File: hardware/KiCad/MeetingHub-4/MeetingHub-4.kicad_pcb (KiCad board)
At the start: 4 copper layers, 265 x 160 mm, 75 parts, among them J1 USB-C POWER IN, J2 TRRS Notebook 1, J3 TRRS Notebook 2, J4 TRRS Notebook 3, J5 TRRS Notebook 4, J6 Headset (User), K1 Select NB1, K2 Select NB2, K3 Select NB3, K4 Select NB4, SW1 MUTE, SW2 Select NB1, SW3 Select NB2, SW4 Select NB3, SW5 Select NB4, U1 NE5532, U2 NJM4556A

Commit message: Resize and relayout
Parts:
- RV1: value 10k Vol NB1 -> Potentiometer_Alps_RK097_Dual_Horizontal; footprint Potentiometer_THT:Potentiometer_Alps_RK097_Dual_Horizontal -> Potentiometer_Alps_RK097_Dual_Horizontal
- RV2: value 10k Vol NB2 -> Potentiometer_Alps_RK097_Dual_Horizontal; footprint Potentiometer_THT:Potentiometer_Alps_RK097_Dual_Horizontal -> Potentiometer_Alps_RK097_Dual_Horizontal
- RV3: value 10k Vol NB3 -> Potentiometer_Alps_RK097_Dual_Horizontal; footprint Potentiometer_THT:Potentiometer_Alps_RK097_Dual_Horizontal -> Potentiometer_Alps_RK097_Dual_Horizontal
- RV4: value 10k Vol NB4 -> Potentiometer_Alps_RK097_Dual_Horizontal; footprint Potentiometer_THT:Potentiometer_Alps_RK097_Dual_Horizontal -> Potentiometer_Alps_RK097_Dual_Horizontal
- RV5: value 10k Master -> Potentiometer_Alps_RK097_Dual_Horizontal; footprint Potentiometer_THT:Potentiometer_Alps_RK097_Dual_Horizontal -> Potentiometer_Alps_RK097_Dual_Horizontal
- SW1: footprint Connector_JST:JST_XH_B2B-XH-A_1x02_P2.50mm_Vertical -> SW_PUSH-12mm
- SW2, SW3, SW4, SW5: footprint Connector_JST:JST_XH_B2B-XH-A_1x02_P2.50mm_Vertical -> SW_CW_GPTS203211B
- moved RV5 155.6 mm to (119.0, 207.4), turned to 90 degrees
- moved C2 124.6 mm to (167.3, 113.5)
- moved D1 118.6 mm to (172.3, 105.4)
- moved J5 113.7 mm to (116.5, 93.7), turned to -90 degrees
- moved C1 113.2 mm to (159.1, 112.3)
- moved F1 110.6 mm to (160.4, 105.0)
- moved MH4 106.1 mm to (215.9, 213.9)
- moved J1 105.7 mm to (165.1, 87.5)
- moved MH2 104.9 mm to (214.1, 91.0)
- moved TP2 90.7 mm to (154.6, 101.8)
- moved C16 88.5 mm to (182.1, 143.8)
- moved J4 86.8 mm to (103.5, 93.7), turned to -90 degrees
- moved R20 84.9 mm to (158.6, 142.5)
- moved C15 84.8 mm to (173.8, 142.5)
- moved R15 84.7 mm to (200.4, 121.8)
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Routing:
- net GND: track 1.06 -> 99.2 mm, vias 5 -> 0
- net NB3_R: track 176.8 -> 78.8 mm
- net NB4_L: track 172.1 -> 81.3 mm, vias 0 -> 1
- net Net-(R12-Pad1): track 153.7 -> 67.0 mm, vias 1 -> 0
- net NB4_R: track 158.5 -> 72.5 mm
- net Net-(R11-Pad1): track 160.4 -> 79.3 mm, vias 1 -> 0
- net Net-(C13-Pad2): track 150.8 -> 74.4 mm
- net Net-(C14-Pad2): track 138.3 -> 68.0 mm
- net Net-(C10-Pad2): track 124.4 -> 55.1 mm
- net Net-(J6-PadR1): track 28.3 -> 96.7 mm
- net Net-(R10-Pad1): track 139.8 -> 73.1 mm, vias 1 -> 0
- net Net-(C11-Pad2): track 140.8 -> 76.5 mm, vias 0 -> 1
- net Net-(SW1-B): track 115.0 -> 57.4 mm
- net Net-(C13-Pad1): track 108.7 -> 166.0 mm
- net Net-(J6-PadT): track 41.7 -> 94.8 mm
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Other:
- board size 265 x 160 mm -> 160.1 x 134 mm

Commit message: jlcpcb production  W2026080810364558  PCB/PCBA
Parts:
- C1, C21, C4: footprint Capacitor_THT:C_Disc_D5.0mm_W2.5mm_P2.50mm -> C_0603_1608Metric
- D1: footprint Diode_THT:D_DO-41_SOD81_P10.16mm_Horizontal -> Nexperia_DSN1608-2_1.6x0.8mm
- RV1: value Potentiometer_Alps_RK097_Dual_Horizontal -> 10k Vol NB1; footprint Potentiometer_Alps_RK097_Dual_Horizontal -> MeetingHub-4:Potentiometer_Alps_RK09L_Double_Vertical
- RV2: value Potentiometer_Alps_RK097_Dual_Horizontal -> 10k Vol NB2; footprint Potentiometer_Alps_RK097_Dual_Horizontal -> MeetingHub-4:Potentiometer_Alps_RK09L_Double_Vertical
- RV3: value Potentiometer_Alps_RK097_Dual_Horizontal -> 10k Vol NB3; footprint Potentiometer_Alps_RK097_Dual_Horizontal -> MeetingHub-4:Potentiometer_Alps_RK09L_Double_Vertical
- RV4: value Potentiometer_Alps_RK097_Dual_Horizontal -> 10k Vol NB4; footprint Potentiometer_Alps_RK097_Dual_Horizontal -> MeetingHub-4:Potentiometer_Alps_RK09L_Double_Vertical
- RV5: footprint Potentiometer_Alps_RK097_Dual_Horizontal -> Potentiometer_THT:Potentiometer_Alps_RK097_Dual_Horizontal
- SW1: footprint SW_PUSH-12mm -> MeetingHub-4:SW_SHOUHAN_TS665ZJ
- SW2, SW3, SW4, SW5: footprint SW_CW_GPTS203211B -> MeetingHub-4:SW_SHOUHAN_TS665ZJ
- moved SW5 41.7 mm to (138.1, 208.2), turned to 0 degrees
- moved RV5 38.6 mm to (157.5, 205.7)
- moved SW4 36.8 mm to (126.0, 208.2), turned to 0 degrees
- moved SW3 34.1 mm to (111.8, 208.3), turned to 0 degrees
- moved SW2 31.8 mm to (99.1, 208.3), turned to 0 degrees
- moved RV2 30.1 mm to (94.6, 162.6)
- moved RV1 20.1 mm to (74.3, 162.6)
- moved RV4 14.9 mm to (135.3, 162.6)
- moved RV3 5.09 mm to (114.9, 162.6)
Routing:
- net Net-(C13-Pad1): track 166.0 -> 92.4 mm
- net Net-(D5-A): track 96.9 -> 41.3 mm, vias 1 -> 0
- net Net-(D4-A): track 90.8 -> 40.7 mm, vias 1 -> 0
- net GND: track 99.2 -> 148.5 mm, vias 0 -> 4
- net Net-(D3-A): track 85.5 -> 37.9 mm, vias 1 -> 0
- net MIX_R: track 48.1 -> 24.1 mm
- net Net-(C12-Pad2): track 76.6 -> 54.1 mm
- net Net-(C13-Pad2): track 74.4 -> 96.9 mm, vias 0 -> 1
- net Net-(D2-A): track 81.2 -> 59.7 mm, vias 1 -> 0
- net Net-(C14-Pad2): track 68.0 -> 88.7 mm, vias 0 -> 1
- net NB4_MIC: track 114.9 -> 96.1 mm
- net Net-(R8-Pad1): track 35.8 -> 54.5 mm
- net Net-(C11-Pad2): track 76.5 -> 59.6 mm, vias 1 -> 0
- net Net-(R6-Pad1): track 35.2 -> 50.3 mm
- net MIX_L: track 96.4 -> 83.6 mm, vias 1 -> 0
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
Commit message: RK09712200HA
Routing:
- net Net-(R8-Pad1): track 54.5 -> 57.3 mm
- net Net-(R10-Pad1): track 68.4 -> 70.8 mm
- net Net-(C13-Pad2): track 96.9 -> 98.5 mm
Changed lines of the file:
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@@
   (footprint "MeetingHub-4:Potentiometer_Alps_RK09L_Double_Vertical" (layer "F.Cu")
     (at 135.265 162.6)
-    (descr "1240015 1240019 12D0A1W 12D0A1T 1240A12 Potentiometer, vertical, Alps RK09L Double, LCSC C380211, https://tech.alpsalpine.com/prod/e/pdf/potentiometer/rotarypotentiometers/rk09l/rk09l.pdf - 2x mechanical MP pads from the official footprint omitted (too close to existing copper on this board), 6 signal pads only")
+    (descr "1240015 1240019 12D0A1W 12D0A1T 1240A12 Potentiometer, vertical, Alps RK09L Double, LCSC C380211, https://tech.alpsalpine.com/prod/e/pdf/potentiometer/rotarypotentiometers/rk09l/rk09l.pdf - 2x mechanical MP pads restored 2026-08-11 (clear of copper after the board relayout; JLCPCB flagged RV1-4 unassembled because the physical part's MP legs had no holes to seat into)")
     (tags "Potentiometer vertical Alps RK09L Double")
     (attr through_hole)
@@
     (pad "6" thru_hole circle (at 2.5 5) (size 1.8 1.8) (drill 1) (layers "*.Cu" "*.Mask")
       (net 3 "VBIAS"))
+    (pad "MP" thru_hole roundrect (at 10 -2.25) (size 2 3) (drill oval 1.1 1.8) (layers "*.Cu" "*.Mask") (roundrect_rratio 0.25))
+    (pad "MP" thru_hole roundrect (at 10 7.25) (size 2 3) (drill oval 1.1 1.8) (layers "*.Cu" "*.Mask") (roundrect_rratio 0.25))
   )
   (footprint "Relay_THT:Relay_SPDT_Omron_G5V-1" (layer "F.Cu")
@@
   (footprint "MeetingHub-4:Potentiometer_Alps_RK09L_Double_Vertical" (layer "F.Cu")
     (at 114.945 162.6)
-    (descr "1240015 1240019 12D0A1W 12D0A1T 1240A12 Potentiometer, vertical, Alps RK09L Double, LCSC C380211, https://tech.alpsalpine.com/prod/e/pdf/potentiometer/rotarypotentiometers/rk09l/rk09l.pdf - 2x mechanical MP pads from the official footprint omitted (too close to existing copper on this board), 6 signal pads only")
+    (descr "1240015 1240019 12D0A1W 12D0A1T 1240A12 Potentiometer, vertical, Alps RK09L Double, LCSC C380211, https://tech.alpsalpine.com/prod/e/pdf/potentiometer/rotarypotentiometers/rk09l/rk09l.pdf - 2x mechanical MP pads restored 2026-08-11 (clear of copper after the board relayout; JLCPCB flagged RV1-4 unassembled because the physical part's MP legs had no holes to seat into)")
     (tags "Potentiometer vertical Alps RK09L Double")
     (attr through_hole)
@@
     (pad "6" thru_hole circle (at 2.5 5) (size 1.8 1.8) (drill 1) (layers "*.Cu" "*.Mask")
       (net 3 "VBIAS"))
+    (pad "MP" thru_hole roundrect (at 10 -2.25) (size 2 3) (drill oval 1.1 1.8) (layers "*.Cu" "*.Mask") (roundrect_rratio 0.25))
+    (pad "MP" thru_hole roundrect (at 10 7.25) (size 2 3) (drill oval 1.1 1.8) (layers "*.Cu" "*.Mask") (roundrect_rratio 0.25))
   )
   (footprint "MeetingHub-4:Potentiometer_Alps_RK09L_Double_Vertical" (layer "F.Cu")
     (at 74.305 162.6)
-    (descr "1240015 1240019 12D0A1W 12D0A1T 1240A12 Potentiometer, vertical, Alps RK09L Double, LCSC C380211, https://tech.alpsalpine.com/prod/e/pdf/potentiometer/rotarypotentiometers/rk09l/rk09l.pdf - 2x mechanical MP pads from the official footprint omitted (too close to existing copper on this board), 6 signal pads only")
+    (descr "1240015 1240019 12D0A1W 12D0A1T 1240A12 Potentiometer, vertical, Alps RK09L Double, LCSC C380211, https://tech.alpsalpine.com/prod/e/pdf/potentiometer/rotarypotentiometers/rk09l/rk09l.pdf - 2x mechanical MP pads restored 2026-08-11 (clear of copper after the board relayout; JLCPCB flagged RV1-4 unassembled because the physical part's MP legs had no holes to seat into)")
     (tags "Potentiometer vertical Alps RK09L Double")
     (attr through_hole)
@@
     (pad "6" thru_hole circle (at 2.5 5) (size 1.8 1.8) (drill 1) (layers "*.Cu" "*.Mask")
       (net 3 "VBIAS"))
+    (pad "MP" thru_hole roundrect (at 10 -2.25) (size 2 3) (drill oval 1.1 1.8) (layers "*.Cu" "*.Mask") (roundrect_rratio 0.25))
+    (pad "MP" thru_hole roundrect (at 10 7.25) (size 2 3) (drill oval 1.1 1.8) (layers "*.Cu" "*.Mask") (roundrect_rratio 0.25))
   )
   (footprint "Relay_THT:Relay_SPDT_Omron_G5V-1" (layer "F.Cu")
@@
   (footprint "MeetingHub-4:Potentiometer_Alps_RK09L_Double_Vertical" (layer "F.Cu")
     (at 94.625 162.6)
-    (descr "1240015 1240019 12D0A1W 12D0A1T 1240A12 Potentiometer, vertical, Alps RK09L Double, LCSC C380211, https://tech.alpsalpine.com/prod/e/pdf/potentiometer/rotarypotentiometers/rk09l/rk09l.pdf - 2x mechanical MP pads from the official footprint omitted (too close to existing copper on this board), 6 signal pads only")
+    (descr "1240015 1240019 12D0A1W 12D0A1T 1240A12 Potentiometer, vertical, Alps RK09L Double, LCSC C380211, https://tech.alpsalpine.com/prod/e/pdf/potentiometer/rotarypotentiometers/rk09l/rk09l.pdf - 2x mechanical MP pads restored 2026-08-11 (clear of copper after the board relayout; JLCPCB flagged RV1-4 unassembled because the physical part's MP legs had no holes to seat into)")
     (tags "Potentiometer vertical Alps RK09L Double")
     (attr through_hole)
@@
     (pad "6" thru_hole circle (at 2.5 5) (size 1.8 1.8) (drill 1) (layers "*.Cu" "*.Mask")
       (net 3 "VBIAS"))
+    (pad "MP" thru_hole roundrect (at 10 -2.25) (size 2 3) (drill oval 1.1 1.8) (layers "*.Cu" "*.Mask") (roundrect_rratio 0.25))
+    (pad "MP" thru_hole roundrect (at 10 7.25) (size 2 3) (drill oval 1.1 1.8) (layers "*.Cu" "*.Mask") (roundrect_rratio 0.25))
   )
   (footprint "Resistor_THT:R_Axial_DIN0207_L6.3mm_D2.5mm_P10.16mm_Horizontal" (layer "F.Cu")
@@
   (segment (start 101.525 142.575) (end 100.45 141.5) (width 0.2) (layer "F.Cu") (net 21))
   (via (at 116.9766 142.575) (size 0.6) (drill 0.3) (layers "F.Cu" "B.Cu") (net 21))
+  (segment (start 124 167) (end 116.9766 160.2966) (width 0.2) (layer "B.Cu") (net 21))
   (segment (start 134.1146 182.3346) (end 134.1146 177.4346) (width 0.2) (layer "B.Cu") (net 21))
   (segment (start 157.52 205.74) (end 134.1146 182.3346) (width 0.2) (layer "B.Cu") (net 21))
   (segment (start 116.9766 160.2966) (end 116.9766 142.575) (width 0.2) (layer "B.Cu") (net 21))
-  (segment (start 134.1146 177.4346) (end 116.9766 160.2966) (width 0.2) (layer "B.Cu") (net 21))
+  (segment (start 127.26 170.58) (end 127.26 167.5) (width 0.2) (layer "B.Cu") (net 21))
+  (segment (start 127.26 167.5) (end 124 167) (width 0.2) (layer "B.Cu") (net 21))
+  (segment (start 134.1146 177.4346) (end 127.26 170.58) (width 0.2) (layer "B.Cu") (net 21))
   (segment (start 140.24 105.3) (end 139.1881 105.3) (width 0.2) (layer "F.Cu") (net 22))
   (segment (start 102.952 141.5) (end 89.3362 127.8842) (width 0.2) (layer "F.Cu") (net 22))
@@
   (segment (start 115.7209 141.111) (end 115.7209 147.0846) (width 0.2) (layer "B.Cu") (net 65))
   (segment (start 115.8697 121.4103) (end 115.8697 140.9622) (width 0.2) (layer "B.Cu") (net 65))
-  (segment (start 115.7209 147.0846) (end 97.7055 165.1) (width 0.2) (layer "B.Cu") (net 65))
+  (segment (start 108 154.806) (end 106.5 163) (width 0.2) (layer "B.Cu") (net 65))
+  (segment (start 106.5 163) (end 97.7055 165.1) (width 0.2) (layer "B.Cu") (net 65))
+  (segment (start 115.7209 147.0846) (end 108 154.806) (width 0.2) (layer "B.Cu") (net 65))
   (segment (start 116.4247 158.2731) (end 116.2667 158.4311) (width 0.2) (layer "B.Cu") (net 66))
   (segment (start 116.4247 141.5774) (end 116.4247 158.2731) (width 0.2) (layer "B.Cu") (net 66))
@@
   (segment (start 116.2666 163.9216) (end 117.445 165.1) (width 0.2) (layer "F.Cu") (net 67))
   (segment (start 75.2001 141.7806) (end 92.8276 159.4081) (width 0.2) (layer "F.Cu") (net 67))
-  (segment (start 92.8276 159.4081) (end 104.9667 159.4081) (width 0.2) (layer "F.Cu") (net 67))
+  (segment (start 92.8276 159.4081) (end 93 163.85) (width 0.2) (layer "F.Cu") (net 67))
   (segment (start 75.2001 127.7001) (end 75.2001 141.7806) (width 0.2) (layer "F.Cu") (net 67))
-  (segment (start 104.9667 159.4081) (end 109.4802 163.9216) (width 0.2) (layer "F.Cu") (net 67))
   (segment (start 109.4802 163.9216) (end 116.2666 163.9216) (width 0.2) (layer "F.Cu") (net 67))
+  (segment (start 93 163.85) (end 109 163.85) (width 0.2) (layer "F.Cu") (net 67))
   (segment (start 73.5 126) (end 75.2001 127.7001) (width 0.2) (layer "F.Cu") (net 67))
+  (segment (start 109 163.85) (end 109.4802 163.9216) (width 0.2) (layer "F.Cu") (net 67))
   (segment (start 106.2778 138.25) (end 119.7981 138.25) (width 0.2) (layer "F.Cu") (net 68))
   (segment (start 94.0278 126) (end 106.2778 138.25) (width 0.2) (layer "F.Cu") (net 68))

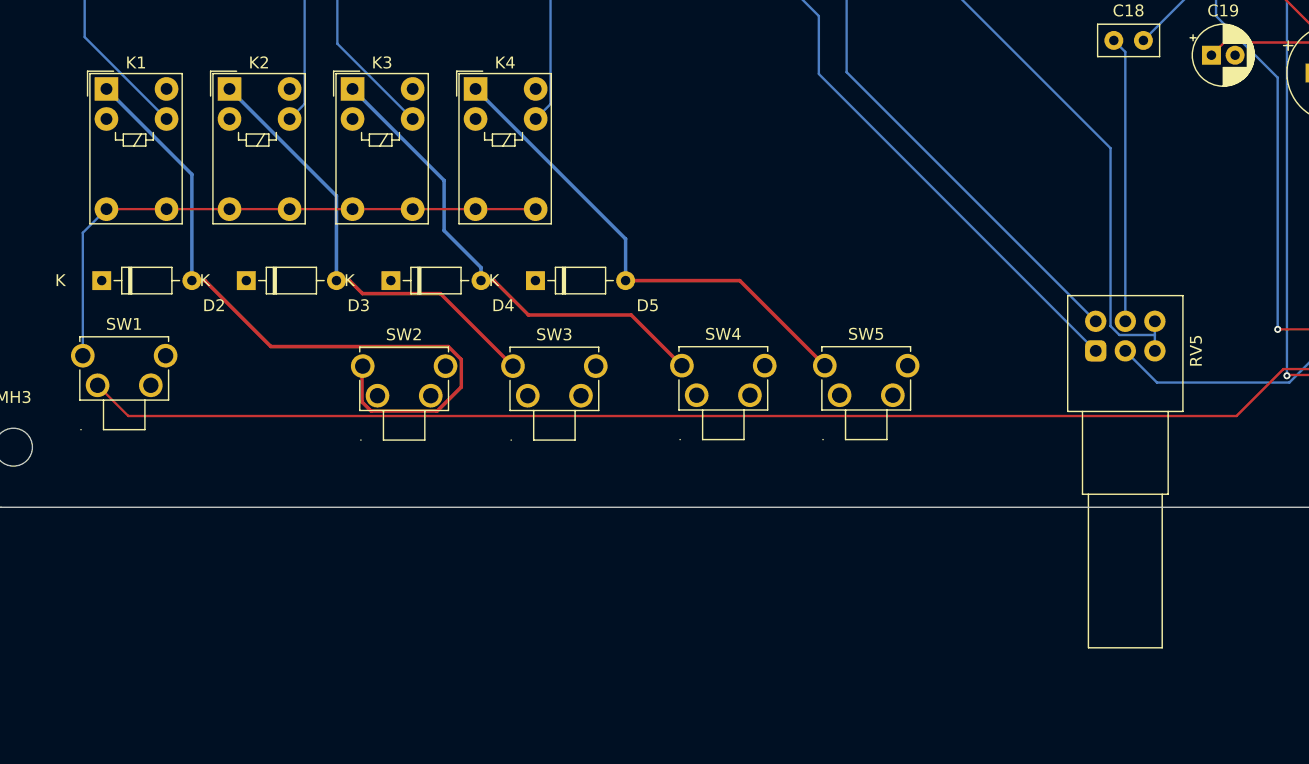
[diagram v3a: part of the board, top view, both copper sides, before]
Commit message: reposition component
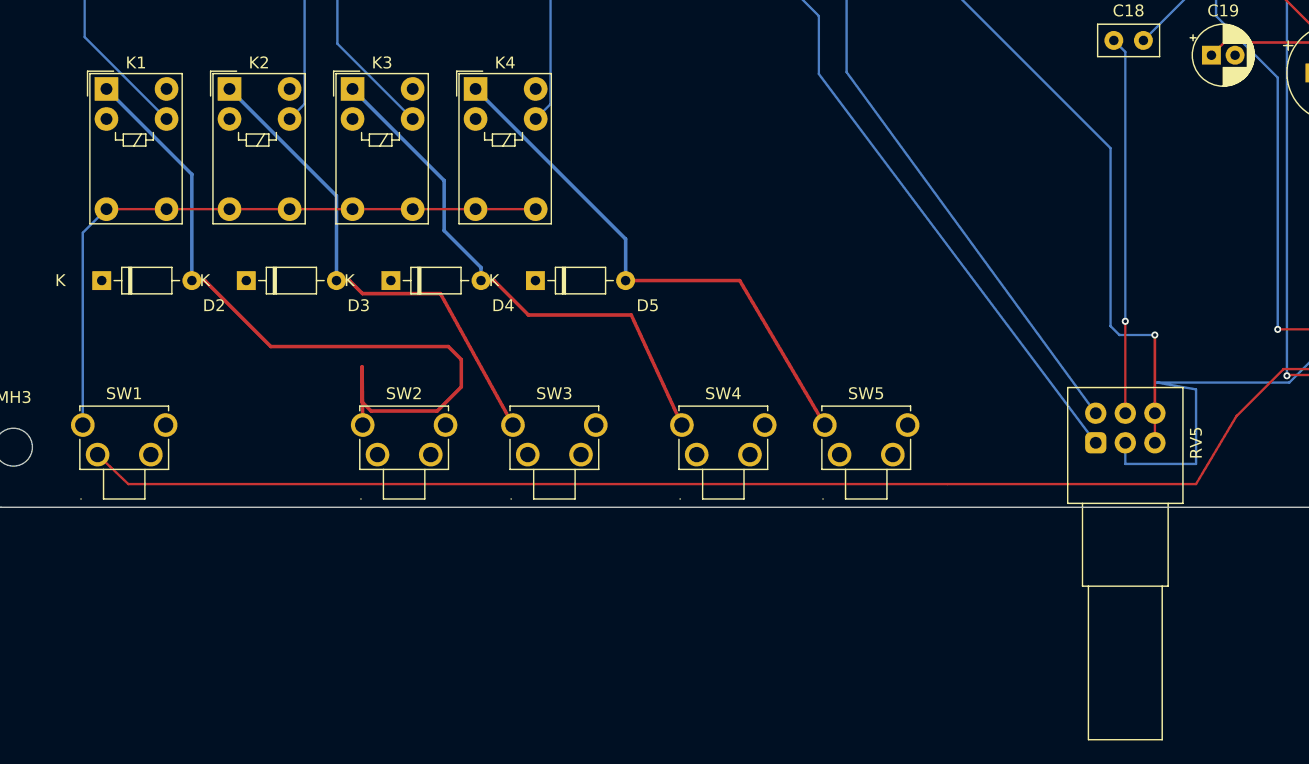
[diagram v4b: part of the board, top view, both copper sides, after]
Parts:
- moved RV5 7.77 mm to (157.5, 213.5)
- moved SW1 5.86 mm to (75.4, 213.3)
- moved SW4 5.02 mm to (126.0, 213.3)
- moved SW5 5.02 mm to (138.1, 213.3)
- moved SW2 4.98 mm to (99.1, 213.3)
- moved SW3 4.98 mm to (111.8, 213.3)
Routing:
- net MIX_L: track 83.6 -> 97.2 mm
- net VBIAS: track 295.6 -> 308.8 mm, vias 1 -> 2
- net MIX_R: track 24.1 -> 31.9 mm, vias 0 -> 1
- net Net-(C14-Pad2): track 88.7 -> 94.6 mm
- net Net-(C13-Pad2): track 98.5 -> 104.4 mm
- net Net-(SW1-B): track 49.5 -> 55.4 mm
- net Net-(D2-A): track 59.7 -> 64.5 mm
- net Net-(D4-A): track 40.7 -> 44.8 mm
- net Net-(D3-A): track 37.9 -> 41.9 mm
- net Net-(D5-A): track 41.3 -> 45.3 mm
- net HEADSET_MIC: track 136.7 -> 139.9 mm
